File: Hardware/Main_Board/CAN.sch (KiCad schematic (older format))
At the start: 5 parts

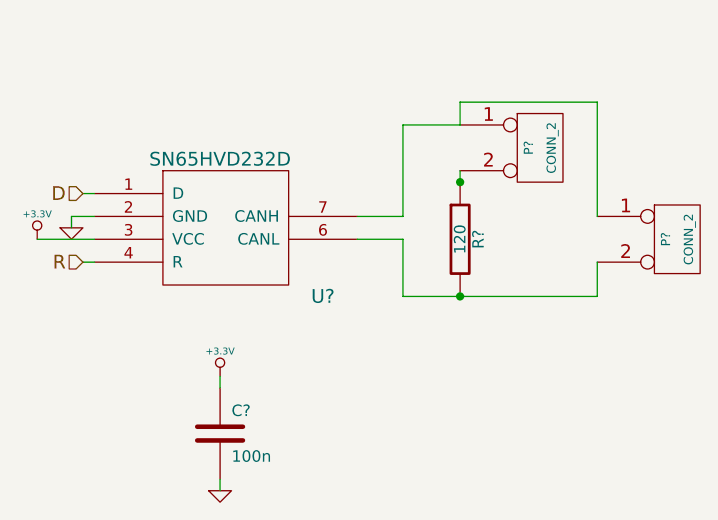
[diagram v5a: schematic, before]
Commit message: [HARDWARE] Component association + schematic modifications
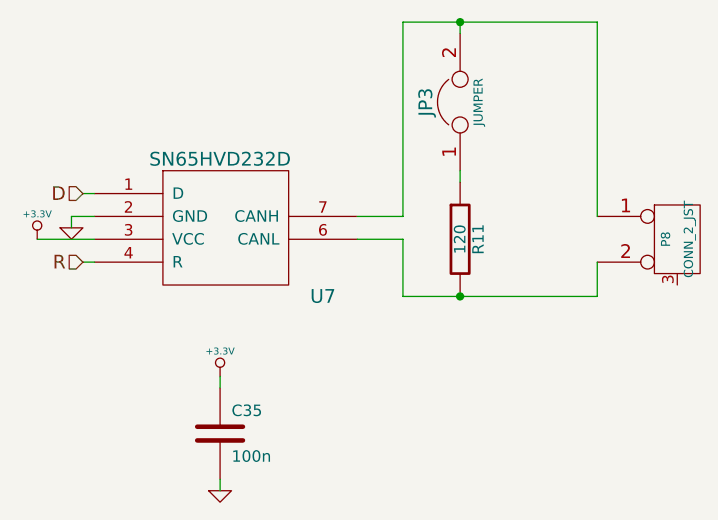
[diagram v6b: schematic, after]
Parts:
- removed P? (x2): CONN_2, symbol CONN_2
- added JP3: JUMPER, symbol JUMPER
- added P8: CONN_2_JST, symbol CONN_2_JST
- gave numbers to parts that had none: 3
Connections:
- net at R11.2, U7.6 (CANL): now also P8.2 (PM)
- net at U7.7 (CANH): now also JP3.2, P8.1 (P1)
- net at R11.1: now also JP3.1
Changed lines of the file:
@@
-EESchema Schematic File Version 2  date jeu. 10 oct. 2013 13:52:33 CEST
+EESchema Schematic File Version 2  date mer. 16 oct. 2013 19:37:53 CEST
 LIBS:power
 LIBS:device
@@
 LIBS:ap1117
 LIBS:l298
+LIBS:conn_4_jst
+LIBS:conn_2_jst
+LIBS:microsd_holder
 LIBS:ausbee-cache
 EELAYER 25  0
@@
 Sheet 6 6
 Title ""
-Date "10 oct 2013"
+Date "16 oct 2013"
 Rev ""
 Comp ""
@@
 Comment4 ""
 $EndDescr
+$Comp
+L CONN_2_JST P8
+U 1 1 525DA201
+P 7300 3550
+F 0 "P8" V 7250 3550 40  0000 C CNN
+F 1 "CONN_2_JST" V 7350 3550 40  0000 C CNN
+	1    7300 3550
+	1    0    0    -1
+$EndComp
+Wire Wire Line
+	6350 3250 6350 3300
+Connection ~ 6350 2600
 Wire Wire Line
 	5300 4200 5300 4150
-Wire Wire Line
-	6350 2950 6350 3050
-Wire Wire Line
-	6350 2950 6950 2950
-Wire Wire Line
-	6950 2950 6950 3450
-Wire Wire Line
-	6350 3250 6350 3300
 Wire Wire Line
 	4750 3650 4700 3650
@@
 Wire Wire Line
 	5900 3450 6100 3450
-Connection ~ 6350 3300
 Wire Wire Line
 	4650 3450 4650 3500
@@
 	4700 3350 4750 3350
 Wire Wire Line
-	6100 3450 6100 3050
+	5300 4650 5300 4600
 Wire Wire Line
-	6100 3050 6350 3050
+	6100 3450 6100 2600
 Wire Wire Line
-	5300 4650 5300 4600
+	6350 2600 6350 2650
+Wire Wire Line
+	6950 3450 6950 2600
+Wire Wire Line
+	6950 2600 6100 2600
 $Comp
-L GND #PWR?
+L JUMPER JP3
+U 1 1 52569CCD
+P 6350 2950
+F 0 "JP3" H 6350 3100 60  0000 C CNN
+F 1 "JUMPER" H 6350 2870 40  0000 C CNN
+	1    6350 2950
+	0    -1   -1   0
+$EndComp
+$Comp
+L GND #PWR153
 U 1 1 52505E54
 P 5300 4650
-F 0 "#PWR?" H 5300 4650 30  0001 C CNN
+F 0 "#PWR153" H 5300 4650 30  0001 C CNN
 F 1 "GND" H 5300 4580 30  0001 C CNN
 	1    5300 4650
@@
 $EndComp
 $Comp
-L +3.3V #PWR?
+L +3.3V #PWR152
 U 1 1 52505E50
 P 5300 4150
-F 0 "#PWR?" H 5300 4110 30  0001 C CNN
+F 0 "#PWR152" H 5300 4110 30  0001 C CNN
 F 1 "+3.3V" H 5300 4260 30  0000 C CNN
 	1    5300 4150
@@
 $EndComp
 $Comp
-L C C?
+L C C35
 U 1 1 52505E43
 P 5300 4400
-F 0 "C?" H 5350 4500 50  0000 L CNN
+F 0 "C35" H 5350 4500 50  0000 L CNN
 F 1 "100n" H 5350 4300 50  0000 L CNN
 	1    5300 4400
-	1    0    0    -1
-$EndComp
-$Comp
-L CONN_2 P?
-U 1 1 52505DE1
-P 6700 3150
-F 0 "P?" V 6650 3150 40  0000 C CNN
-F 1 "CONN_2" V 6750 3150 40  0000 C CNN
-	1    6700 3150
 	1    0    0    -1
 $EndComp
@@
 D
 $Comp
-L +3.3V #PWR?
+L +3.3V #PWR150
 U 1 1 52505D30
 P 4500 3550
-F 0 "#PWR?" H 4500 3510 30  0001 C CNN
+F 0 "#PWR150" H 4500 3510 30  0001 C CNN
 F 1 "+3.3V" H 4500 3660 30  0000 C CNN
 	1    4500 3550
@@
 $EndComp
 $Comp
-L GND #PWR?
+L GND #PWR151
 U 1 1 52505D28
 P 4650 3500
-F 0 "#PWR?" H 4650 3500 30  0001 C CNN
+F 0 "#PWR151" H 4650 3500 30  0001 C CNN
 F 1 "GND" H 4650 3430 30  0001 C CNN
 	1    4650 3500
@@
 $EndComp
 $Comp
-L CONN_2 P?
-U 1 1 52505D1B
-P 7300 3550
-F 0 "P?" V 7250 3550 40  0000 C CNN
-F 1 "CONN_2" V 7350 3550 40  0000 C CNN
-	1    7300 3550
-	1    0    0    -1
-$EndComp
-$Comp
-L R R?
+L R R11
 U 1 1 52505D04
 P 6350 3550
-F 0 "R?" V 6430 3550 50  0000 C CNN
+F 0 "R11" V 6430 3550 50  0000 C CNN
 F 1 "120" V 6350 3550 50  0000 C CNN
 	1    6350 3550
@@
 $EndComp
 $Comp
-L SN65HVD232D U?
+L SN65HVD232D U7
 U 1 1 52505CC2
 P 5300 3500
-F 0 "U?" H 5750 3200 60  0000 C CNN
+F 0 "U7" H 5750 3200 60  0000 C CNN
 F 1 "SN65HVD232D" H 5300 3800 60  0000 C CNN
 	1    5300 3500

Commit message: [HARDWARE] Update schematic and start routing
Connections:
- net GND: now also P8.3
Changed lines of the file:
@@
-EESchema Schematic File Version 2  date mer. 16 oct. 2013 19:37:53 CEST
+EESchema Schematic File Version 2  date dim. 20 oct. 2013 18:50:44 CEST
 LIBS:power
 LIBS:device
@@
 Sheet 6 6
 Title ""
-Date "16 oct 2013"
+Date "20 oct 2013"
 Rev ""
 Comp ""
@@
 Comment4 ""
 $EndDescr
+Wire Wire Line
+	7300 3800 7300 3750
+Wire Wire Line
+	6950 2600 6100 2600
+Wire Wire Line
+	6950 2600 6950 3450
+Wire Wire Line
+	6350 2600 6350 2650
+Wire Wire Line
+	6100 2600 6100 3450
+Wire Wire Line
+	5300 4650 5300 4600
+Wire Wire Line
+	4700 3350 4750 3350
+Wire Wire Line
+	4750 3550 4500 3550
+Wire Wire Line
+	4650 3500 4650 3450
+Wire Wire Line
+	6100 3450 5900 3450
+Wire Wire Line
+	6100 3550 6100 3800
+Wire Wire Line
+	6100 3550 5900 3550
+Wire Wire Line
+	6100 3800 6950 3800
+Wire Wire Line
+	6950 3800 6950 3650
+Connection ~ 6350 3800
+Wire Wire Line
+	4650 3450 4750 3450
+Wire Wire Line
+	4750 3650 4700 3650
+Wire Wire Line
+	5300 4200 5300 4150
+Connection ~ 6350 2600
+Wire Wire Line
+	6350 3250 6350 3300
+$Comp
+L GND #PWR149
+U 1 1 52616784
+P 7300 3800
+F 0 "#PWR149" H 7300 3800 30  0001 C CNN
+F 1 "GND" H 7300 3730 30  0001 C CNN
+	1    7300 3800
+	1    0    0    -1
+$EndComp
 $Comp
 L CONN_2_JST P8
@@
 	1    0    0    -1
 $EndComp
-Wire Wire Line
-	6350 3250 6350 3300
-Connection ~ 6350 2600
-Wire Wire Line
-	5300 4200 5300 4150
-Wire Wire Line
-	4750 3650 4700 3650
-Wire Wire Line
-	4750 3450 4650 3450
-Connection ~ 6350 3800
-Wire Wire Line
-	6950 3650 6950 3800
-Wire Wire Line
-	6950 3800 6100 3800
-Wire Wire Line
-	5900 3550 6100 3550
-Wire Wire Line
-	6100 3550 6100 3800
-Wire Wire Line
-	5900 3450 6100 3450
-Wire Wire Line
-	4650 3450 4650 3500
-Wire Wire Line
-	4750 3550 4500 3550
-Wire Wire Line
-	4700 3350 4750 3350
-Wire Wire Line
-	5300 4650 5300 4600
-Wire Wire Line
-	6100 3450 6100 2600
-Wire Wire Line
-	6350 2600 6350 2650
-Wire Wire Line
-	6950 3450 6950 2600
-Wire Wire Line
-	6950 2600 6100 2600
 $Comp
 L JUMPER JP3
@@
 $EndComp
 $Comp
-L GND #PWR153
+L GND #PWR148
 U 1 1 52505E54
 P 5300 4650
-F 0 "#PWR153" H 5300 4650 30  0001 C CNN
+F 0 "#PWR148" H 5300 4650 30  0001 C CNN
 F 1 "GND" H 5300 4580 30  0001 C CNN
 	1    5300 4650
@@
 $EndComp
 $Comp
-L +3.3V #PWR152
+L +3.3V #PWR147
 U 1 1 52505E50
 P 5300 4150
-F 0 "#PWR152" H 5300 4110 30  0001 C CNN
+F 0 "#PWR147" H 5300 4110 30  0001 C CNN
 F 1 "+3.3V" H 5300 4260 30  0000 C CNN
 	1    5300 4150
@@
 D
 $Comp
-L +3.3V #PWR150
+L +3.3V #PWR145
 U 1 1 52505D30
 P 4500 3550
-F 0 "#PWR150" H 4500 3510 30  0001 C CNN
+F 0 "#PWR145" H 4500 3510 30  0001 C CNN
 F 1 "+3.3V" H 4500 3660 30  0000 C CNN
 	1    4500 3550
@@
 $EndComp
 $Comp
-L GND #PWR151
+L GND #PWR146
 U 1 1 52505D28
 P 4650 3500
-F 0 "#PWR151" H 4650 3500 30  0001 C CNN
+F 0 "#PWR146" H 4650 3500 30  0001 C CNN
 F 1 "GND" H 4650 3430 30  0001 C CNN
 	1    4650 3500
